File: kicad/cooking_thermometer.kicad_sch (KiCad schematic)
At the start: 41 parts, among them J1 FTDI, J2 STLINK, J3 3V3_Power, J4 Battery, J5 7SEG_CONN, J6 OLED_CONN, J7 USB_B_Micro, J8 THERMO_CONN, Q1 BC547, SW1 BOOT0_SW, SW2 NRST_SW, SW3 UI_A_SW, SW4 UI_B_SW, SW5 UI_C_SW, U1 STM32F070F6Px, U2 MCP1700x-330xxTO, U3 MCP73831-2-OT

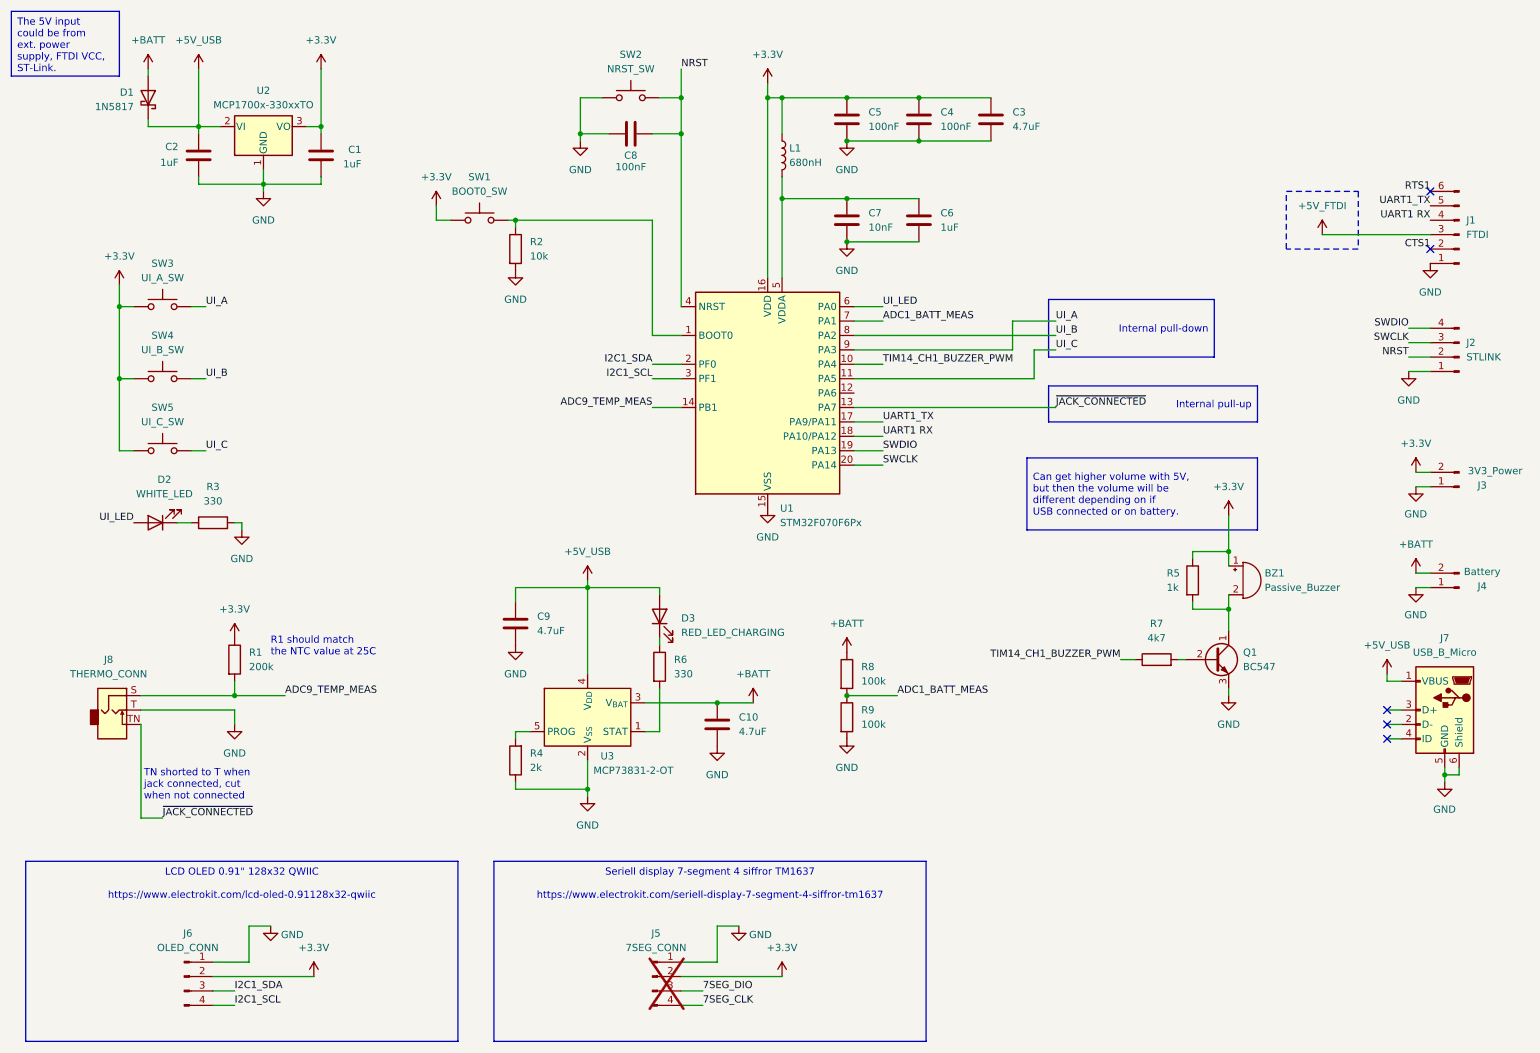
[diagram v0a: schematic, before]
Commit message: Edit schematic for nrf52810
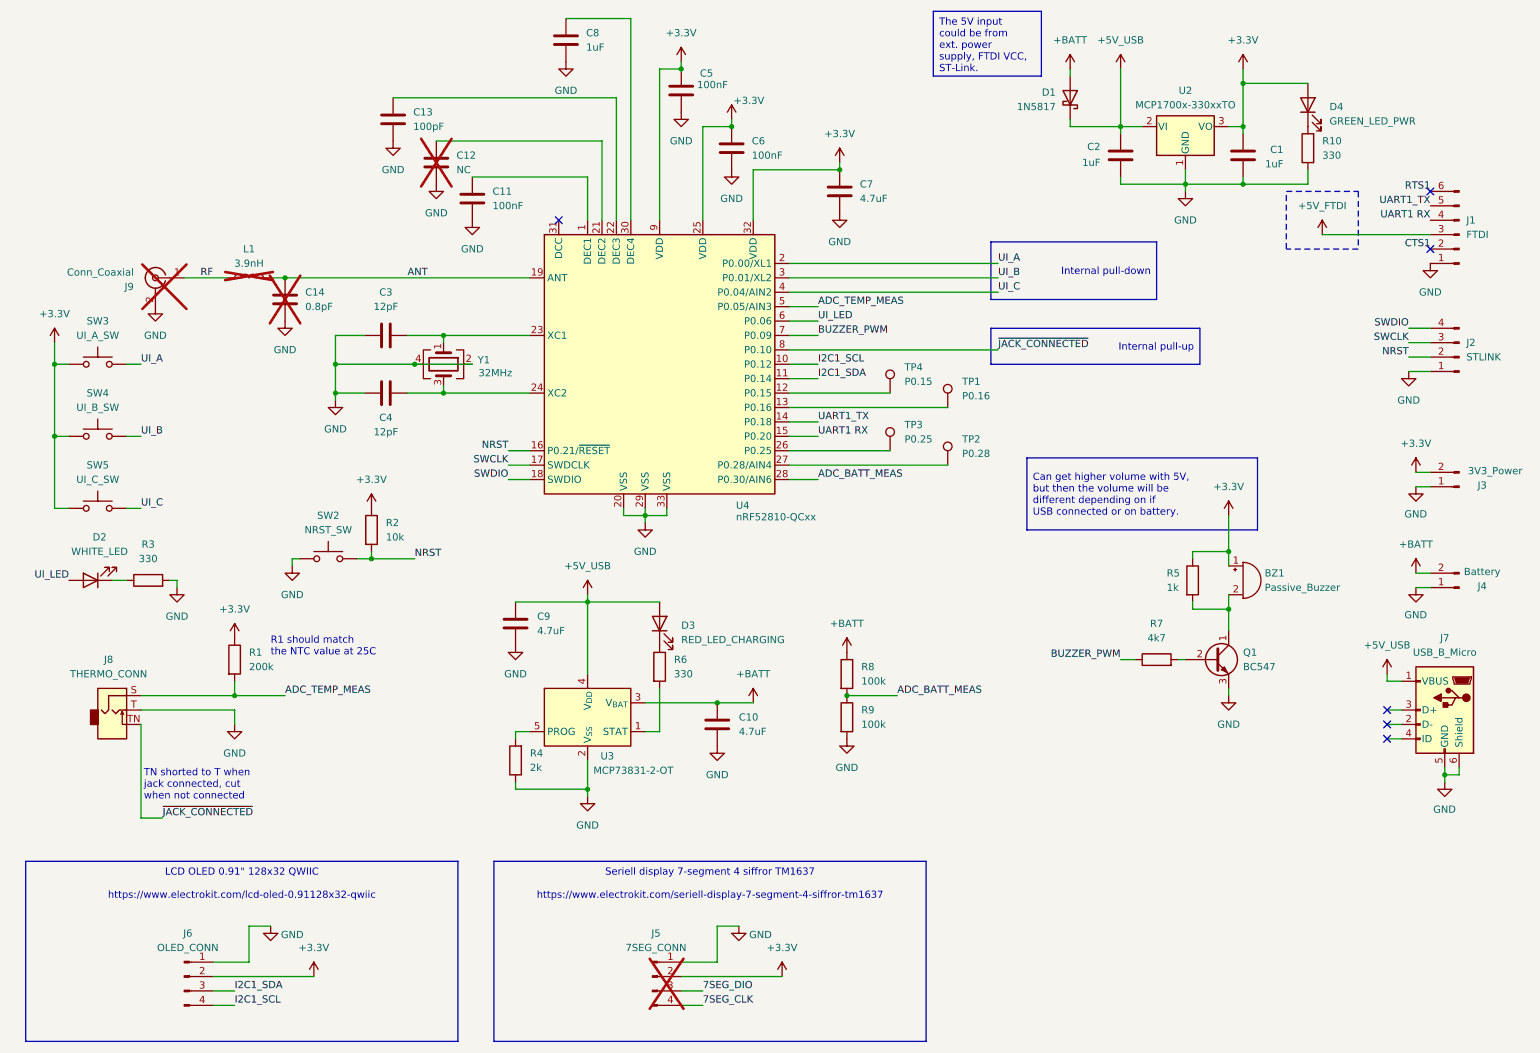
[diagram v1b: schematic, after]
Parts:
- removed SW1: BOOT0_SW, Button_Switch_THT:SW_PUSH_6mm, symbol Switch:SW_Push
- removed U1: STM32F070F6Px, MyOwnFootprintLibrary:STM32F070_DIP20, symbol MCU_ST_STM32F0:STM32F070F6Px
- added C11: 100nF, Capacitor_SMD:C_1206_3216Metric_Pad1.33x1.80mm_HandSolder, symbol Device:C
- added C12: NC, Capacitor_SMD:C_1206_3216Metric_Pad1.33x1.80mm_HandSolder, symbol Device:C
- added C13: 100pF, Capacitor_SMD:C_1206_3216Metric_Pad1.33x1.80mm_HandSolder, symbol Device:C
- added C14: 0.8pF, Capacitor_SMD:C_1206_3216Metric_Pad1.33x1.80mm_HandSolder, symbol Device:C
- added D4: GREEN_LED_PWR, LED_THT:LED_Rectangular_W5.0mm_H2.0mm, symbol Device:LED
- added J9: Conn_Coaxial, Connector_Coaxial:U.FL_Molex_MCRF_73412-0110_Vertical, symbol Connector:Conn_Coaxial
- added R10: 330, Resistor_SMD:R_1206_3216Metric_Pad1.30x1.75mm_HandSolder, symbol Device:R
- added TP1: P0.16, TestPoint:TestPoint_Pad_D2.0mm, symbol Connector:TestPoint
- added TP2: P0.28, TestPoint:TestPoint_Pad_D2.0mm, symbol Connector:TestPoint
- added TP3: P0.25, TestPoint:TestPoint_Pad_D2.0mm, symbol Connector:TestPoint
- added TP4: P0.15, TestPoint:TestPoint_Pad_D2.0mm, symbol Connector:TestPoint
- added U4: nRF52810-QCxx, Package_DFN_QFN:QFN-32-1EP_5x5mm_P0.5mm_EP3.6x3.6mm_ThermalVias, symbol MCU_Nordic:nRF52810-QCxx
- added Y1: 32MHz, Crystal:Crystal_SMD_3225-4Pin_3.2x2.5mm_HandSoldering, symbol Device:Crystal_GND24
- C1, C10, C2, C5, C9: footprint Capacitor_THT:C_Disc_D3.0mm_W1.6mm_P2.50mm -> Capacitor_SMD:C_1206_3216Metric_Pad1.33x1.80mm_HandSolder
- C3: value 4.7uF -> 12pF; footprint Capacitor_THT:C_Disc_D3.0mm_W1.6mm_P2.50mm -> Capacitor_SMD:C_1206_3216Metric_Pad1.33x1.80mm_HandSolder
- C4: value 100nF -> 12pF; footprint Capacitor_THT:C_Disc_D3.0mm_W1.6mm_P2.50mm -> Capacitor_SMD:C_1206_3216Metric_Pad1.33x1.80mm_HandSolder
- C6: value 1uF -> 100nF; footprint Capacitor_THT:C_Disc_D3.0mm_W1.6mm_P2.50mm -> Capacitor_SMD:C_1206_3216Metric_Pad1.33x1.80mm_HandSolder
- C7: value 10nF -> 4.7uF; footprint Capacitor_THT:C_Disc_D3.0mm_W1.6mm_P2.50mm -> Capacitor_SMD:C_1206_3216Metric_Pad1.33x1.80mm_HandSolder
- C8: value 100nF -> 1uF; footprint Capacitor_THT:C_Disc_D3.0mm_W1.6mm_P2.50mm -> Capacitor_SMD:C_1206_3216Metric_Pad1.33x1.80mm_HandSolder
- D3: footprint LED_THT:LED_D4.0mm -> LED_THT:LED_Rectangular_W5.0mm_H2.0mm
- L1: value 680nH -> 3.9nH; footprint Inductor_THT:L_Axial_L12.0mm_D5.0mm_P15.24mm_Horizontal_Fastron_MISC -> Inductor_SMD:L_1206_3216Metric_Pad1.22x1.90mm_HandSolder; now not fitted
- Q1: footprint Package_TO_SOT_THT:TO-92L_Inline_Wide -> Package_TO_SOT_THT:TO-92L_Inline
- R1, R2, R3, R4, R6, R8, R9: footprint Resistor_THT:R_Axial_DIN0207_L6.3mm_D2.5mm_P10.16mm_Horizontal -> Resistor_SMD:R_1206_3216Metric_Pad1.30x1.75mm_HandSolder
- R5, R7: footprint Resistor_THT:R_Axial_DIN0207_L6.3mm_D2.5mm_P7.62mm_Horizontal -> Resistor_SMD:R_1206_3216Metric_Pad1.30x1.75mm_HandSolder
- U2: footprint Package_TO_SOT_THT:TO-92_Inline_Wide -> Package_TO_SOT_THT:TO-92L_Inline
- U3: footprint MyOwnFootprintLibrary:DIP-5-6_7.62mm_5on6 -> Package_TO_SOT_SMD:SOT-23-5_HandSoldering
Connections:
- net +3.3V: now also C5.2, C6.2, C7.2, R2.1, D4.2 (A), U4.25 (VDD), U4.32 (VDD), U4.9 (VDD); no longer C3.1, C4.1, C5.1, L1.1
- net GND: now also C3.1, C5.1, C6.1, C7.1, C11.1, C12.1, C13.1, C14.1, J9.2 (Ext), R10.1, U4.20 (VSS), U4.29 (VSS), U4.33 (VSS), Y1.2, Y1.4; no longer C3.2, C5.2, C6.2, C7.2, R2.2
- net I2C1_SCL: now also U4.10 (P0.12)
- net I2C1_SDA: now also U4.11 (P0.14)
- net NRST: now also R2.2, U4.16 (P0.21/~{RESET}); no longer C8.2
- net SWCLK: now also U4.17 (SWDCLK)
- net SWDIO: now also U4.18 (SWDIO)
- net UART1 RX: now also U4.15 (P0.20)
- net UART1_TX: now also U4.14 (P0.18)
- net UI_A: now also U4.2 (P0.00/XL1)
- net UI_B: now also U4.3 (P0.01/XL2)
- net UI_C: now also U4.4 (P0.04/AIN2)
- net UI_LED: now also U4.6 (P0.06)
- net ~{JACK_CONNECTED}: now also U4.8 (P0.10)
- net ADC1_BATT_MEAS renamed ADC_BATT_MEAS
- net ADC_BATT_MEAS: now also U4.28 (P0.30/AIN6)
- net ADC9_TEMP_MEAS renamed ADC_TEMP_MEAS
- net ADC_TEMP_MEAS: now also U4.5 (P0.05/AIN3)
- net TIM14_CH1_BUZZER_PWM renamed BUZZER_PWM
- net BUZZER_PWM: now also U4.7 (P0.09)
- new net: C12.2, U4.21 (DEC2)
- new net: TP1.1, U4.13 (P0.16)
- new net: C11.2, U4.1 (DEC1)
- new net: TP2.1, U4.27 (P0.28/AIN4)
- new net: C3.2, U4.23 (XC1), Y1.1
- new net: D4.1 (K), R10.2
- new net: C4.1, U4.24 (XC2), Y1.3
- new net: TP4.1, U4.12 (P0.15)
- new net: C8.2, U4.30 (DEC4)
- new net: TP3.1, U4.26 (P0.25)
- new net: C13.2, U4.22 (DEC3)
- new net ANT: C14.2, L1.2, U4.19 (ANT)
- new net RF: J9.1 (In), L1.1
- no-connect marks 5 -> 6
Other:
- moved on the sheet: C1, C2, D1, D2, D3, R3, SW2, SW3, SW4, SW5, U2
